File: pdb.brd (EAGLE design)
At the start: 50 x 100 mm, 50 parts, among them J1 XT60PWFEMALE, Q1 IRFR5305PBF, Q2 IRFR5305PBF, Q3 20MHz, U1 TSR_1-2433, U2 TXB0104, U3 ATMEGA48-20AU, U4 LTC2946CMSPBF, U5 LTC2946CMSPBF, U6 LTC2946CMSPBF, U7 AT30TS74SS8M

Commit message: silkscreen
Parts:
- removed U$3: BSN20,215, jonas_mosfet:BSN20_215
- added XTAL1: 20MHz, crystal:HC49UP
- Q3: value 20MHz -> BSN20,215; device crystal:HC49UP -> jonas_mosfet:BSN20_215
- moved Q3 21.7 mm to (25.0, 35.0), turned to 180 degrees
- renumbered U$1 to Q4, U$2 to Q5
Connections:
- net GND: now also Q3.2; no longer U$3.2
- net N$11: now also Q3.3; no longer U$3.3
- net N$27: now also XTAL1.2; no longer Q3.2
- net N$28: now also XTAL1.1; no longer Q3.1
- net RST_H: now also Q3.1; no longer U$3.1

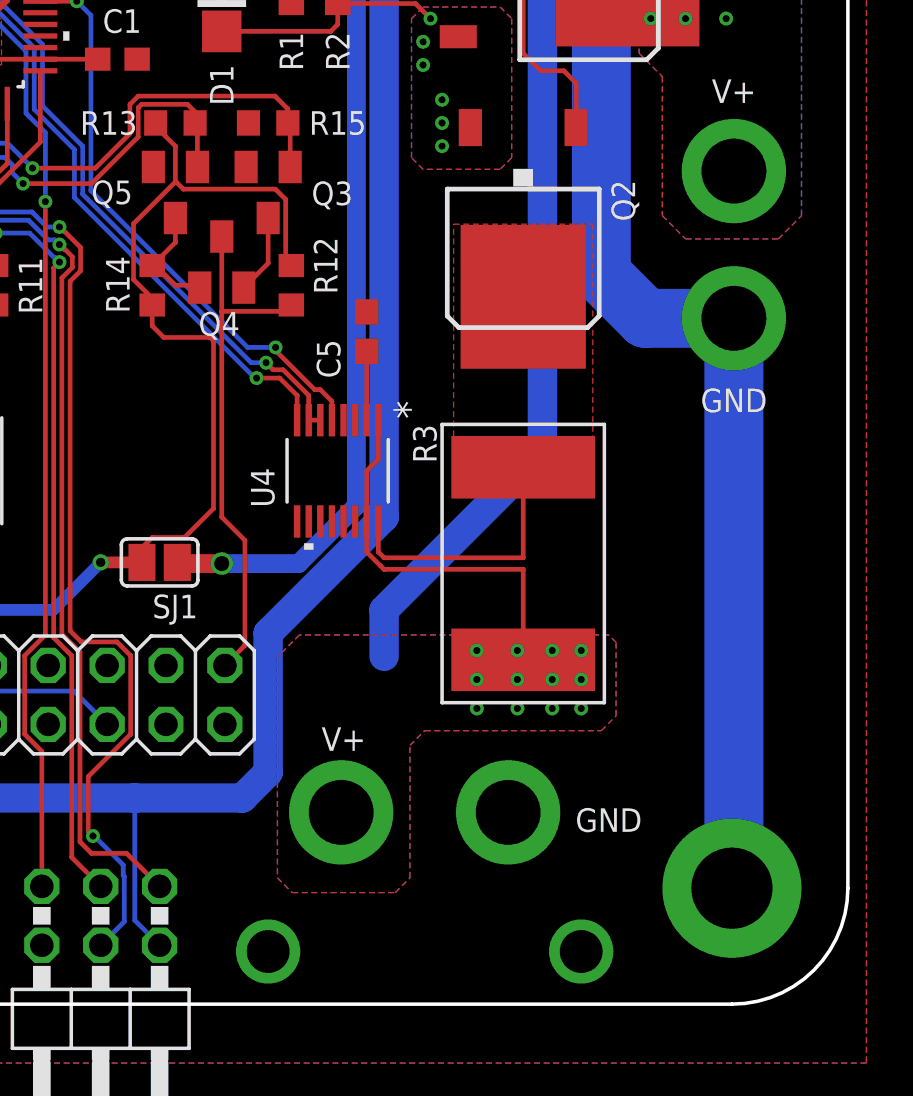
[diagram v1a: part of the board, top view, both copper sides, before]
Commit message: fixed layout, silkscreen, resistor values
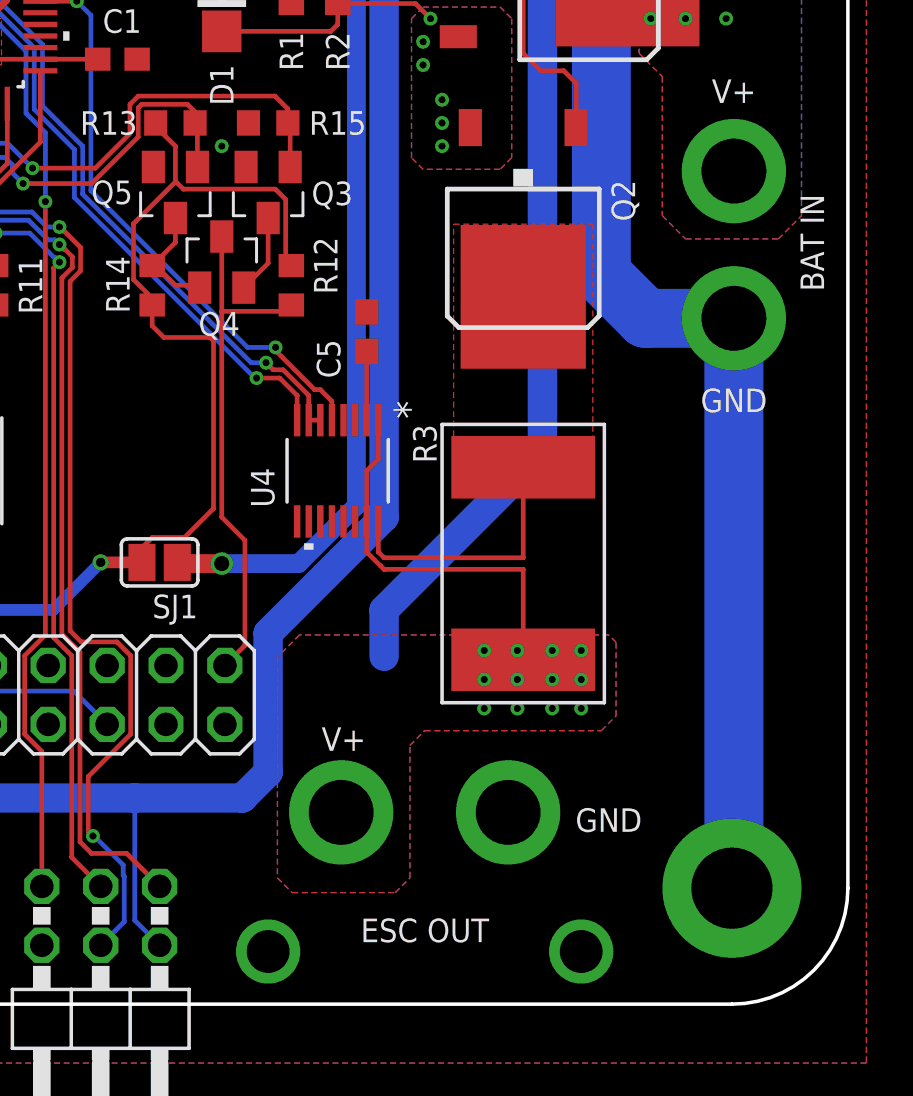
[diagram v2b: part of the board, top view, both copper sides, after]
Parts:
- R12, R14, R15: value 4k7 -> 10k
- R13: value 4K7 -> 10k
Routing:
- net GND: vias 32 -> 33
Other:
- board text added: "BAT IN"
- board text added: "ESC OUT"
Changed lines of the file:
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@@
 <setting verticaltext="up"/>
 </settings>
-<grid distance="1" unitdist="mm" unit="mm" style="lines" multiple="1" display="yes" altdistance="0.125" altunitdist="mm" altunit="mm"/>
+<grid distance="1" unitdist="mm" unit="mm" style="lines" multiple="1" display="yes" altdistance="0.25" altunitdist="mm" altunit="mm"/>
 <layers>
 <layer number="1" name="Top" color="4" fill="1" visible="yes" active="yes"/>
@@
 <layer number="49" name="Reference" color="60" fill="1" visible="no" active="yes"/>
 <layer number="50" name="dxf" color="7" fill="1" visible="no" active="no"/>
-<layer number="51" name="tDocu" color="7" fill="1" visible="yes" active="yes"/>
-<layer number="52" name="bDocu" color="7" fill="1" visible="yes" active="yes"/>
+<layer number="51" name="tDocu" color="7" fill="1" visible="no" active="yes"/>
+<layer number="52" name="bDocu" color="7" fill="1" visible="no" active="yes"/>
 <layer number="53" name="tGND_GNDA" color="7" fill="1" visible="no" active="no"/>
 <layer number="54" name="bGND_GNDA" color="7" fill="1" visible="no" active="no"/>
@@
 <text x="45.085" y="39.37" size="1.016" layer="21" align="center">V+</text>
 <text x="28.2575" y="11.43" size="1.016" layer="21" align="center">V+</text>
+<text x="48.465" y="32.835" size="1.016" layer="21" rot="R90" align="center">BAT IN</text>
+<text x="31.7575" y="3.18" size="1.016" layer="21" align="center">ESC OUT</text>
 </plain>
 <attributes>
@@
 </class>
 </classes>
-<designrules name="FusionPCB *">
+<designrules name="FusionPCB">
 <description language="de">&lt;b&gt;FUSION PCB Rules&lt;/b&gt;
 &lt;p&gt;
@@
 <attribute name="VALUE" x="19.685" y="86.36" size="1.27" layer="27" rot="R90"/>
 </element>
-<element name="R14" library="rcl" library_urn="urn:adsk.eagle:library:334" package="R0603" package3d_urn="urn:adsk.eagle:package:23555/2" value="4k7" x="20" y="31" smashed="yes" rot="R270">
+<element name="R14" library="rcl" library_urn="urn:adsk.eagle:library:334" package="R0603" package3d_urn="urn:adsk.eagle:package:23555/2" value="10k" x="20" y="31" smashed="yes" rot="R270">
 <attribute name="NAME" x="18.01" y="32.26" size="1.016" layer="25" rot="R270"/>
 <attribute name="SPICEPREFIX" value="R" x="20" y="31" size="1.778" layer="27" rot="R270" display="off"/>
 <attribute name="VALUE" x="18.095" y="31.635" size="1.27" layer="27" rot="R270"/>
 </element>
-<element name="R12" library="rcl" library_urn="urn:adsk.eagle:library:334" package="R0603" package3d_urn="urn:adsk.eagle:package:23555/2" value="4k7" x="26" y="31" smashed="yes" rot="R90">
+<element name="R12" library="rcl" library_urn="urn:adsk.eagle:library:334" package="R0603" package3d_urn="urn:adsk.eagle:package:23555/2" value="10k" x="26" y="31" smashed="yes" rot="R90">
 <attribute name="NAME" x="27.99" y="30.615" size="1.016" layer="25" rot="R90"/>
 <attribute name="SPICEPREFIX" value="R" x="26" y="31" size="1.778" layer="27" rot="R90" display="off"/>
 <attribute name="VALUE" x="27.905" y="30.365" size="1.27" layer="27" rot="R90"/>
 </element>
-<element name="R13" library="rcl" library_urn="urn:adsk.eagle:library:334" package="R0603" package3d_urn="urn:adsk.eagle:package:23555/2" value="4K7" x="21" y="38" smashed="yes" rot="R180">
+<element name="R13" library="rcl" library_urn="urn:adsk.eagle:library:334" package="R0603" package3d_urn="urn:adsk.eagle:package:23555/2" value="10k" x="21" y="38" smashed="yes" rot="R180">
 <attribute name="NAME" x="18.125" y="38" size="1.016" layer="25" align="center"/>
 <attribute name="SPICEPREFIX" value="R" x="21" y="38" size="1.778" layer="27" rot="R180" display="off"/>
 <attribute name="VALUE" x="21.635" y="39.905" size="1.27" layer="27" rot="R180"/>
 </element>
-<element name="R15" library="rcl" library_urn="urn:adsk.eagle:library:334" package="R0603" package3d_urn="urn:adsk.eagle:package:23555/2" value="4k7" x="25" y="38" smashed="yes">
+<element name="R15" library="rcl" library_urn="urn:adsk.eagle:library:334" package="R0603" package3d_urn="urn:adsk.eagle:package:23555/2" value="10k" x="25" y="38" smashed="yes">
 <attribute name="NAME" x="28" y="38" size="1.016" layer="25" align="center"/>
 <attribute name="SPICEPREFIX" value="R" x="25" y="38" size="1.778" layer="27" display="off"/>
 <attribute name="VALUE" x="24.365" y="36.095" size="1.27" layer="27"/>
 </element>
-<element name="Q4" library="jonas_mosfet" library_urn="urn:adsk.eagle:library:2195717" package="BSN20_215" package3d_urn="urn:adsk.eagle:package:2195720/3" value="BSN20,215" x="21" y="35" smashed="yes" rot="R180">
+<element name="Q4" library="jonas_mosfet" library_urn="urn:adsk.eagle:library:2195717" package="BSN20_215" package3d_urn="urn:adsk.eagle:package:2195720/4" value="BSN20,215" x="21" y="35" smashed="yes" rot="R180">
 <attribute name="AVAILABILITY" value="Good" x="21" y="35" size="1.778" layer="27" rot="R180" display="off"/>
 <attribute name="DESCRIPTION" value="BSN Series 50 V 15 Ohm 0.83 W N-Channel Enhancement Mode Transistor - SOT-23" x="21" y="35" size="1.778" layer="27" rot="R180" display="off"/>
@@
 <attribute name="PRICE" value="0.17 USD" x="21" y="35" size="1.778" layer="27" rot="R180" display="off"/>
 </element>
-<element name="Q5" library="jonas_mosfet" library_urn="urn:adsk.eagle:library:2195717" package="BSN20_215" package3d_urn="urn:adsk.eagle:package:2195720/3" value="BSN20,215" x="23" y="32" smashed="yes">
+<element name="Q5" library="jonas_mosfet" library_urn="urn:adsk.eagle:library:2195717" package="BSN20_215" package3d_urn="urn:adsk.eagle:package:2195720/4" value="BSN20,215" x="23" y="32" smashed="yes">
 <attribute name="AVAILABILITY" value="Good" x="23" y="32" size="1.778" layer="27" display="off"/>
 <attribute name="DESCRIPTION" value="BSN Series 50 V 15 Ohm 0.83 W N-Channel Enhancement Mode Transistor - SOT-23" x="23" y="32" size="1.778" layer="27" display="off"/>
@@
 <attribute name="PRICE" value="0.17 USD" x="23" y="32" size="1.778" layer="27" display="off"/>
 </element>
-<element name="Q3" library="jonas_mosfet" library_urn="urn:adsk.eagle:library:2195717" package="BSN20_215" package3d_urn="urn:adsk.eagle:package:2195720/3" value="BSN20,215" x="25" y="35" smashed="yes" rot="R180">
+<element name="Q3" library="jonas_mosfet" library_urn="urn:adsk.eagle:library:2195717" package="BSN20_215" package3d_urn="urn:adsk.eagle:package:2195720/4" value="BSN20,215" x="25" y="35" smashed="yes" rot="R180">
 <attribute name="AVAILABILITY" value="Good" x="25" y="35" size="1.778" layer="27" rot="R180" display="off"/>
 <attribute name="DESCRIPTION" value="BSN Series 50 V 15 Ohm 0.83 W N-Channel Enhancement Mode Transistor - SOT-23" x="25" y="35" size="1.778" layer="27" rot="R180" display="off"/>
@@
 <contactref element="Q3" pad="2"/>
 <contactref element="Q4" pad="2"/>
+<via x="23" y="37" extent="1-16" drill="0.3"/>
 </signal>
 <signal name="V+">
@@
 <vertex x="25.4" y="5.445"/>
 </polygon>
-<via x="34" y="15.25" extent="1-16" drill="0.3"/>
+<via x="34.3175" y="15.25" extent="1-16" drill="0.3"/>
 <via x="35.75" y="15.25" extent="1-16" drill="0.3"/>
 <via x="37.25" y="15.25" extent="1-16" drill="0.3"/>
@@
 <via x="37.25" y="14" extent="1-16" drill="0.3"/>
 <via x="35.75" y="14" extent="1-16" drill="0.3"/>
-<via x="34" y="14" extent="1-16" drill="0.3"/>
-<via x="34" y="12.75" extent="1-16" drill="0.3"/>
+<via x="34.3175" y="14" extent="1-16" drill="0.3"/>
+<via x="34.3175" y="12.75" extent="1-16" drill="0.3"/>
 <via x="35.75" y="12.75" extent="1-16" drill="0.3"/>
 <via x="37.25" y="12.75" extent="1-16" drill="0.3"/>

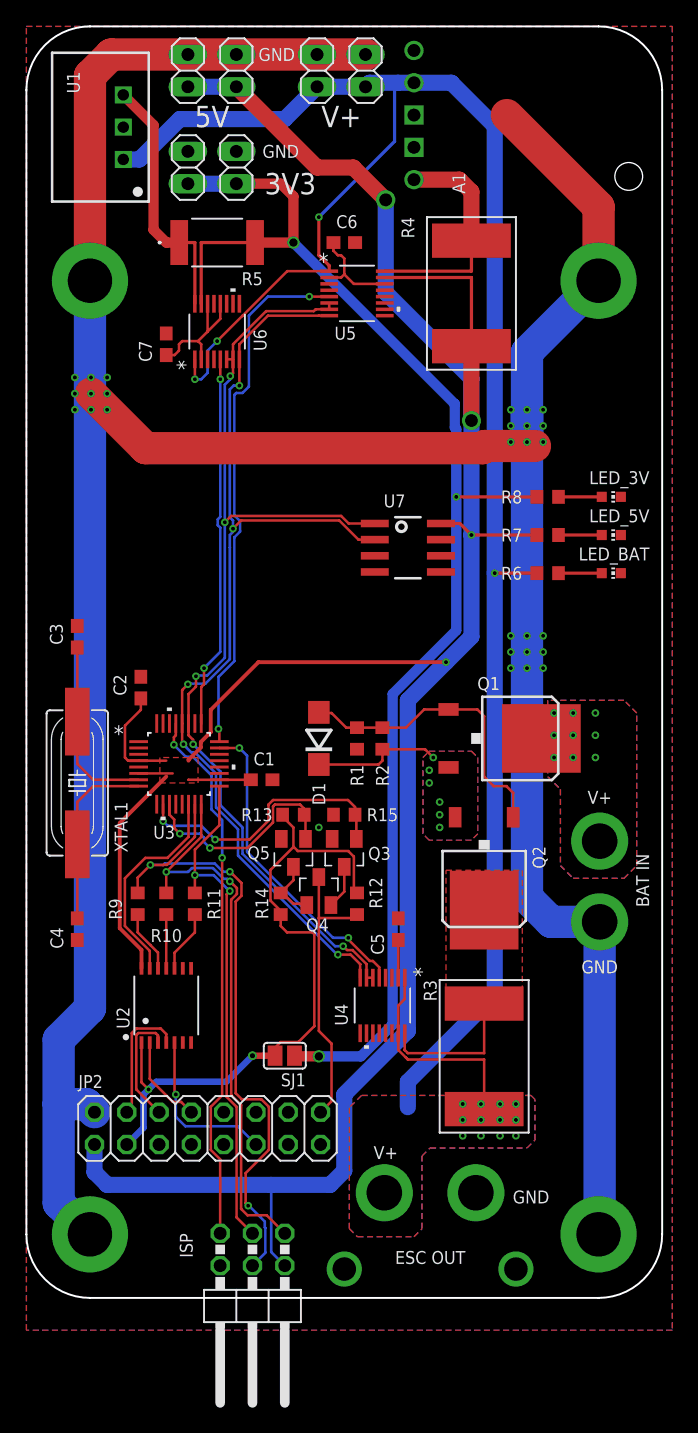
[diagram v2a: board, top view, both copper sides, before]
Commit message: changed LTC2946 for easier soldering
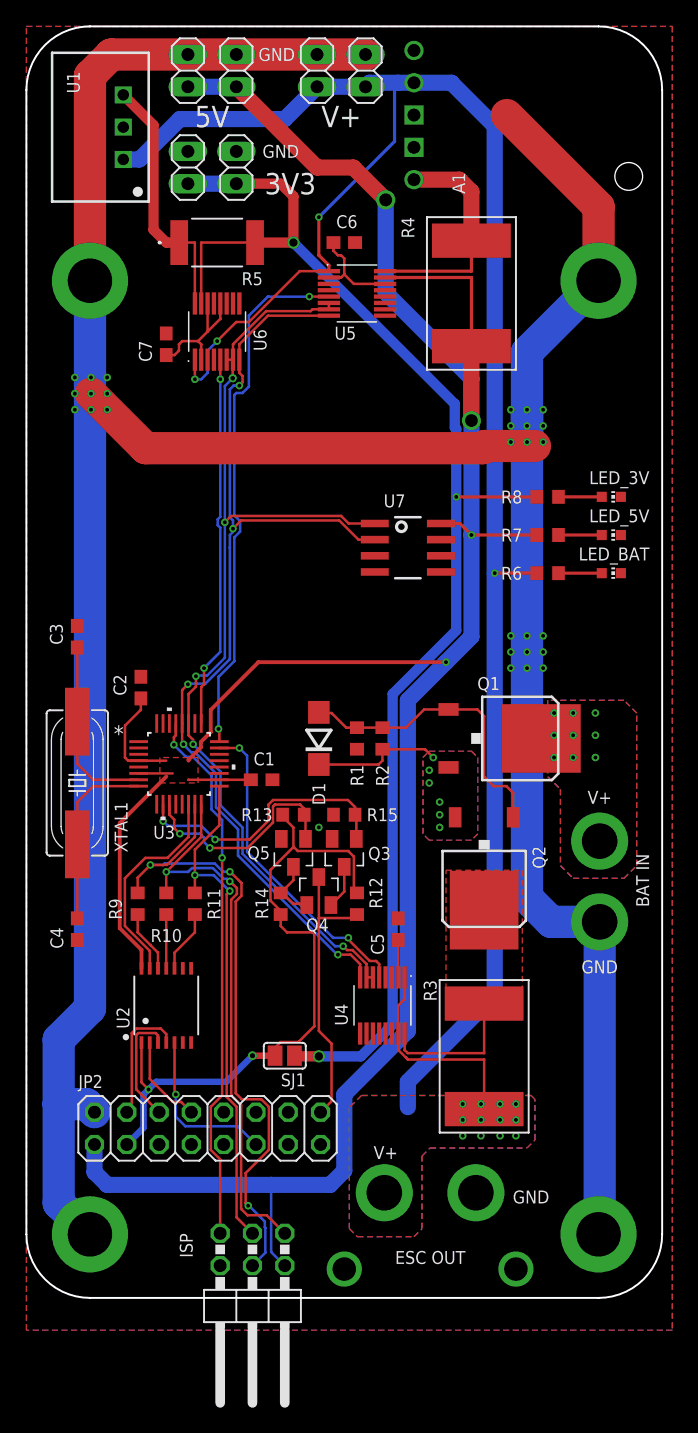
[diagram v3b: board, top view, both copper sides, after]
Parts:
- U4, U5, U6: device niklas_lt:MSOP-16_MS -> linear:SOP50P489X110-16

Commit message: fixed atmega
closes #12
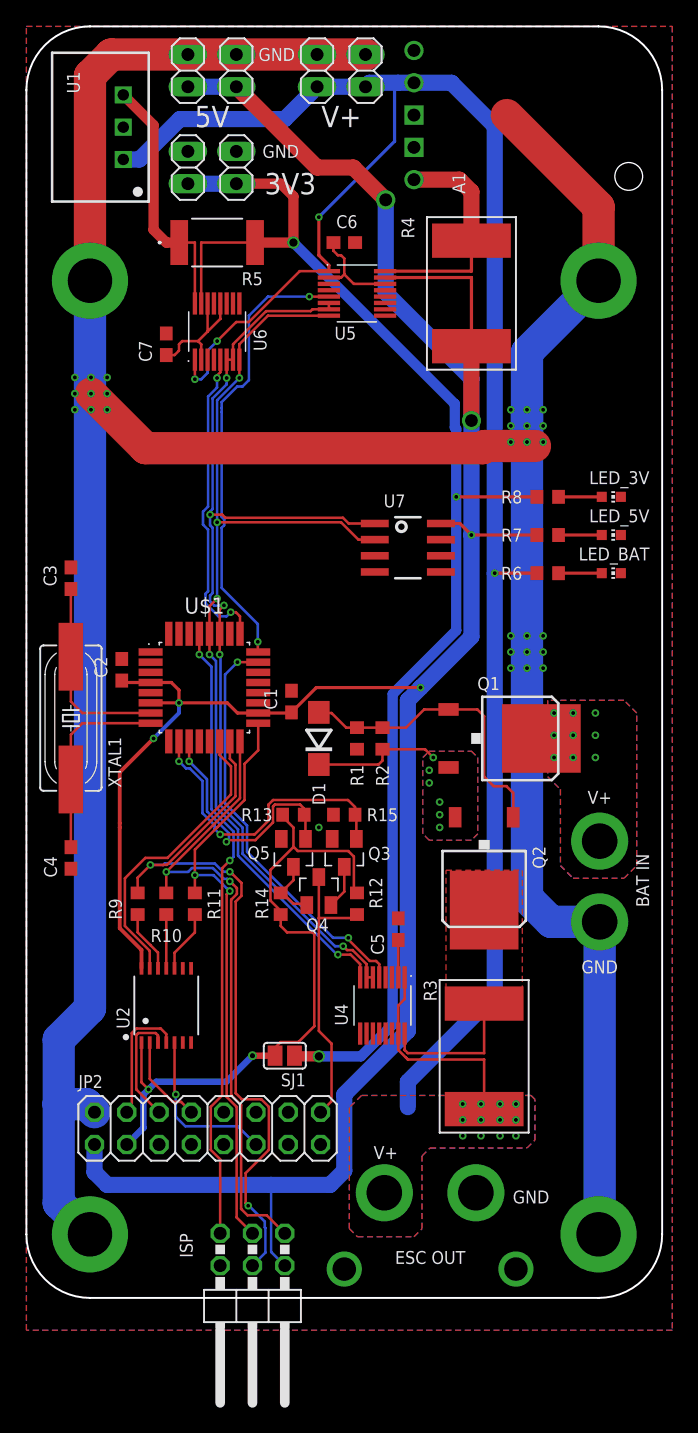
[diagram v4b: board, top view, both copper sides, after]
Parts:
- removed U3: ATMEGA48-20AU, niklas_atmel:32A
- added U$1: ATMEGA48-20AU, jonas_atmel:QFP80P900X900X120-32
- moved C1 6.58 mm to (20.9, 46.9), turned to 90 degrees
- moved C4 5.62 mm to (3.50, 34.6)
- moved XTAL1 5.12 mm to (3.50, 45.6)
- moved C3 4.63 mm to (3.50, 56.6)
- moved C2 2.05 mm to (7.50, 49.4)
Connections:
- net !ALERT_3V3: now also U$1.25; no longer U3.25
- net !ALERT_5V: now also U$1.24; no longer U3.24
- net !ALERT_V+: now also U$1.23; no longer U3.23
- net +5V: now also U$1.18, U$1.4, U$1.6; no longer U3.18, U3.4, U3.6
- net GND: now also U$1.21, U$1.3, U$1.5; no longer U3.21, U3.3, U3.5
- net MISO_5V: now also U$1.16; no longer U3.16
- net MOSI_5V: now also U$1.15; no longer U3.15
- net N$27: now also U$1.7; no longer U3.7
- net N$28: now also U$1.8; no longer U3.8
- net RESET: now also U$1.29; no longer U3.29
- net RST_H: now also U$1.10; no longer U3.10
- net RST_L: now also U$1.11; no longer U3.11
- net SCK_5V: now also U$1.17; no longer U3.17
- net SCL: now also U$1.28; no longer U3.28
- net SDA: now also U$1.27; no longer U3.27
- net SS_5V: now also U$1.14; no longer U3.14
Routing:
- net !ALERT_V+: track 25.2 -> 32.8 mm
- net SS_5V: track 16.8 -> 23.5 mm
- net RESET: track 42.7 -> 49.3 mm
- net +5V: track 216.2 -> 209.7 mm, vias 4 -> 6
- net MOSI_5V: track 51.6 -> 58.0 mm
- net !ALERT_5V: track 42.1 -> 35.9 mm
- net SCK_5V: track 40.3 -> 46.5 mm
- net MISO_5V: track 44.4 -> 50.6 mm
- net !ALERT_3V3: track 29.5 -> 24.8 mm
- net SCL: track 79.7 -> 77.2 mm
- net RST_H: track 21.8 -> 24.1 mm
- net RST_L: track 17.8 -> 19.9 mm
- net N$28: track 14.5 -> 15.5 mm
- net N$27: track 14.5 -> 15.5 mm
- removed copper zone on layer 1, net +5V
